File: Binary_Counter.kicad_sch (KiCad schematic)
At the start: 12 parts, among them SW1 SW_Push, U1 CH32V003FxUx

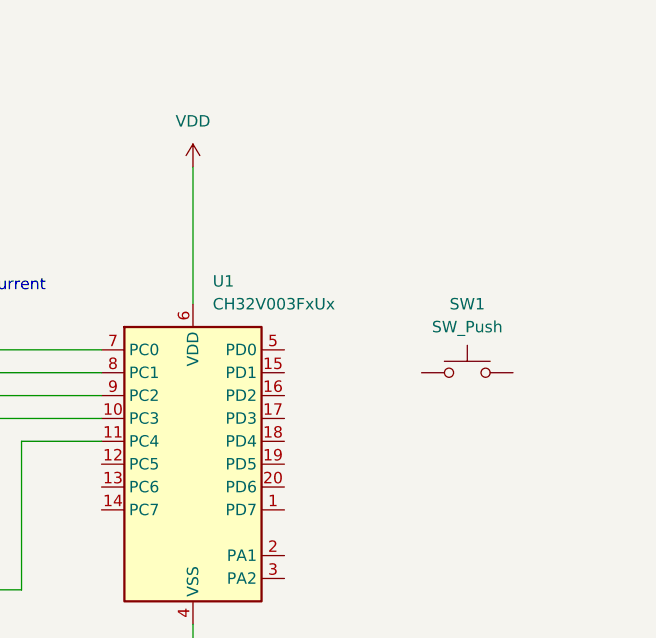
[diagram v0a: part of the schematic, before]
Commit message: move switch to PD2, add debouncing to switch
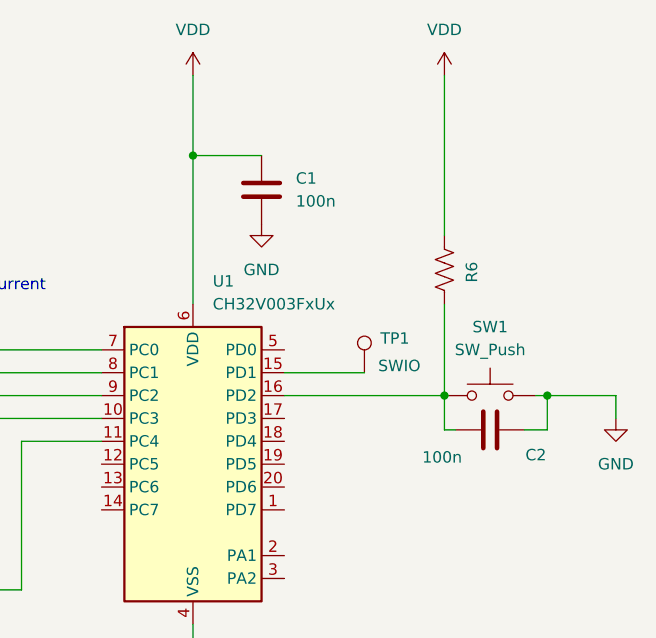
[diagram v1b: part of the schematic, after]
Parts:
- added C1, C2: 100n, symbol Device:C
- added R6: R_US, symbol Device:R_US
- added TP1: SWIO, symbol Connector:TestPoint
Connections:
- net GND: now also SW1.2, C1.2, C2.2
- net VDD: now also C1.1, R6.1
- net at SW1.1: now also U1.16 (PD2), C2.1, R6.2
- net at U1.15 (PD1): now also TP1.1

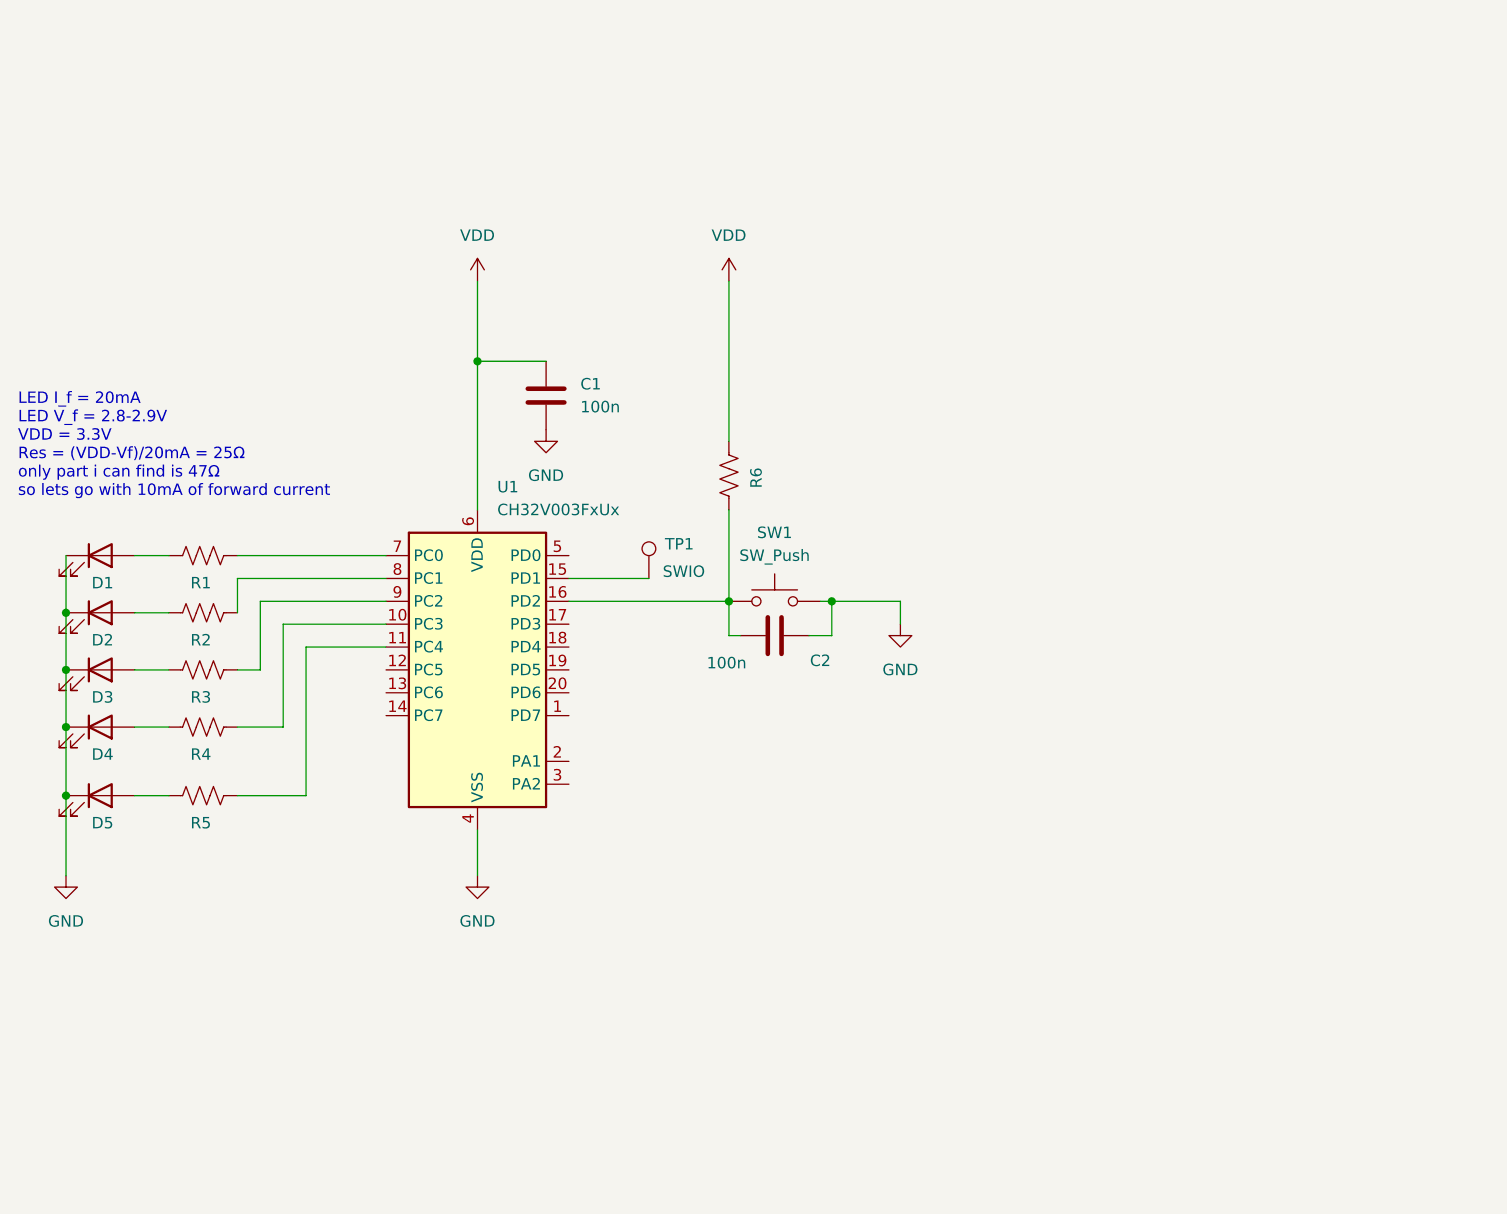
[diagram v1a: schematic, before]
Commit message: add 8 LEDs total and add a 3 pin connector for power and SWIO
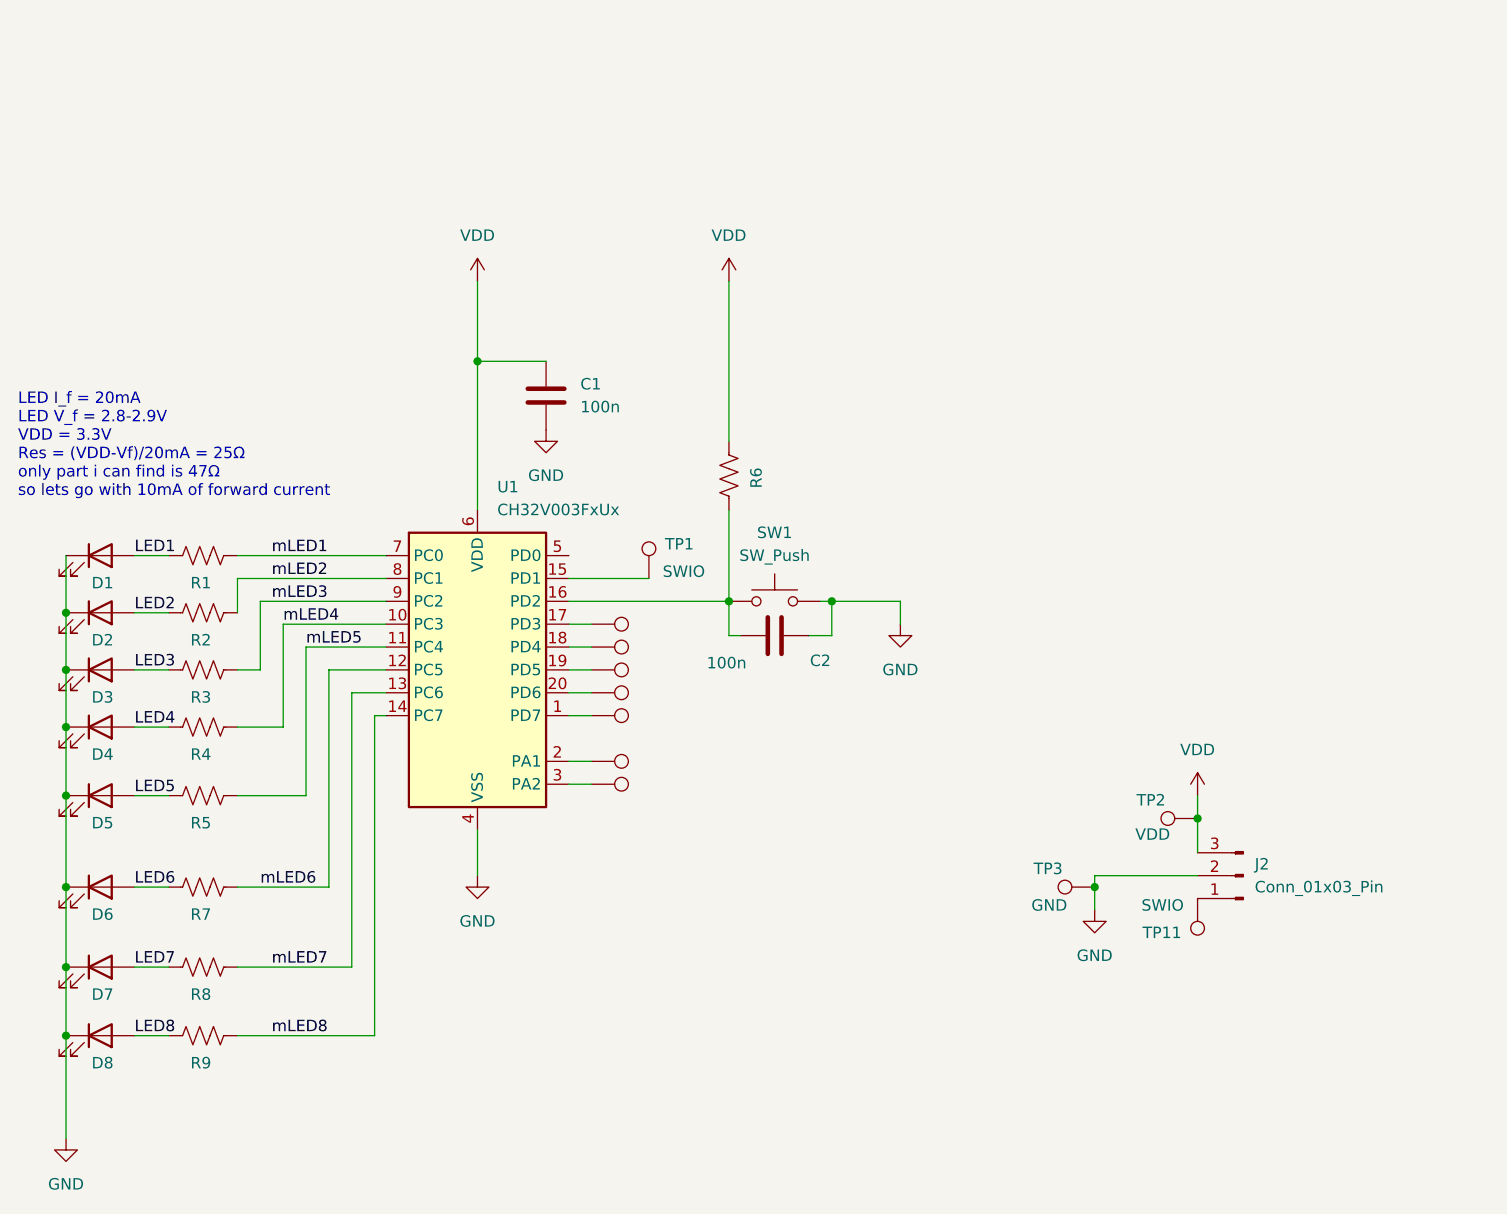
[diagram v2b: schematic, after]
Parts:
- added D6, D7, D8: LED, symbol Device:LED
- added J2: Conn_01x03_Pin, symbol Connector:Conn_01x03_Pin
- added R7, R8, R9: R_US, symbol Device:R_US
- added TP10, TP11, TP4, TP5, TP6, TP7, TP8, TP9: SWIO, symbol Connector:TestPoint
- added TP2: VDD, symbol Connector:TestPoint
- added TP3: GND, symbol Connector:TestPoint
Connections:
- net GND: now also D6.1 (K), D7.1 (K), D8.1 (K), J2.2 (Pin_2), TP3.1
- net VDD: now also J2.3 (Pin_3), TP2.1
- net LED4: now reaches D4.2 (A), R4.2
- net LED3: now reaches D3.2 (A), R3.2
- net mLED5: now reaches R5.1, U1.11 (PC4)
- net LED5: now reaches D5.2 (A), R5.2
- net mLED2: now reaches R2.1, U1.8 (PC1)
- net LED2: now reaches D2.2 (A), R2.2
- net LED1: now reaches D1.2 (A), R1.2
- net mLED4: now reaches R4.1, U1.10 (PC3)
- net mLED3: now reaches R3.1, U1.9 (PC2)
- net mLED1: now reaches R1.1, U1.7 (PC0)
- net at U1.1 (PD7): now also TP8.1
- net mLED6: now reaches U1.12 (PC5)
- net mLED6: now also R7.1
- net mLED7: now reaches U1.13 (PC6)
- net mLED7: now also R8.1
- net mLED8: now reaches U1.14 (PC7)
- net mLED8: now also R9.1
- net at U1.17 (PD3): now also TP4.1
- net at U1.18 (PD4): now also TP5.1
- net at U1.19 (PD5): now also TP6.1
- net at U1.2 (PA1): now also TP9.1
- net at U1.20 (PD6): now also TP7.1
- net at U1.3 (PA2): now also TP10.1
- new net: J2.1 (Pin_1), TP11.1
- new net LED6: D6.2 (A), R7.2
- new net LED7: D7.2 (A), R8.2
- new net LED8: D8.2 (A), R9.2

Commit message: initial placement of components on board
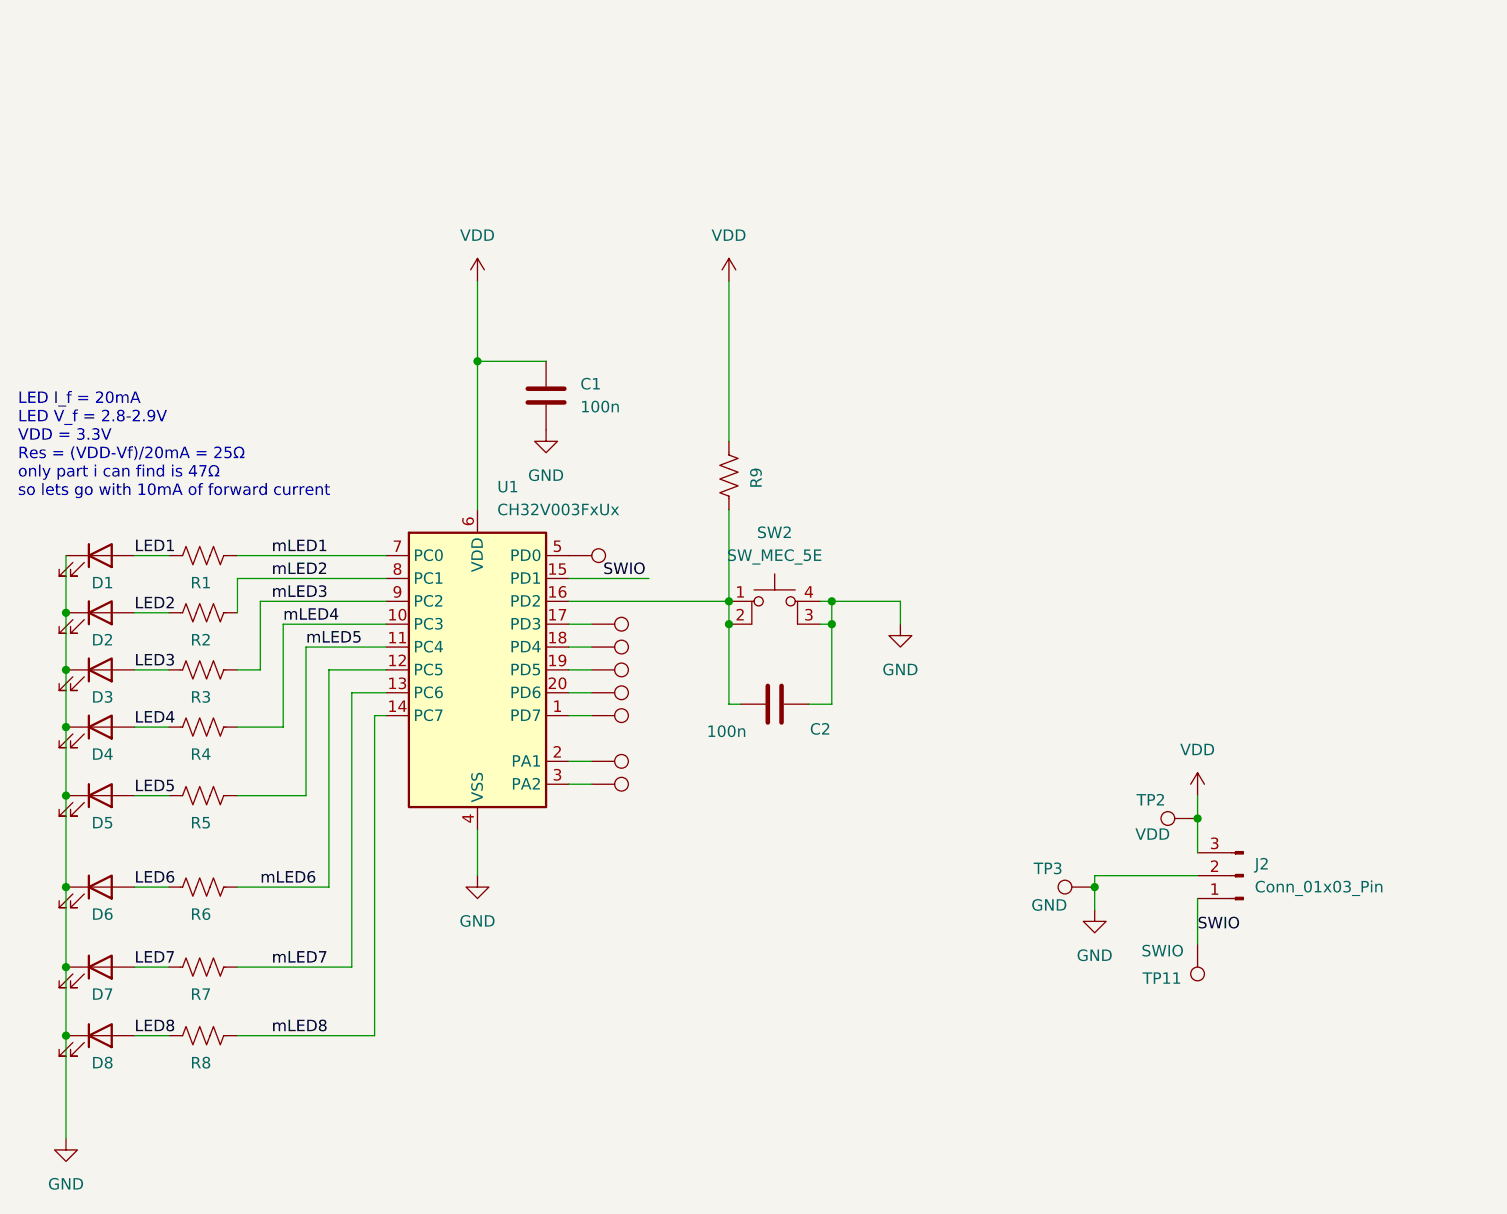
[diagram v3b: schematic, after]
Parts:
- removed SW1: SW_Push, symbol Switch:SW_Push
- removed TP1: SWIO, symbol Connector:TestPoint
- added SW2: SW_MEC_5E, TACT Switch:SW-SMD_4P-L5.1-W5.1-P3.70-LS6.5-TL-2, symbol Switch:SW_MEC_5E
- added TP12: PD0, TestPoint:TestPoint_Pad_D2.0mm, symbol Connector:TestPoint
- C1, C2: footprint (none) -> Capacitor_SMD:C_0805_2012Metric_Pad1.18x1.45mm_HandSolder
- D1, D2, D3, D4, D5, D6, D7, D8: footprint (none) -> LED:LED0805-R-RD
- J2: footprint (none) -> Connector:FanPinHeader_1x03_P2.54mm_Vertical
- R1, R2, R3, R4, R5: footprint (none) -> Resistor_SMD:R_0805_2012Metric_Pad1.20x1.40mm_HandSolder
- R6: renamed from R7; footprint (none) -> Resistor_SMD:R_0805_2012Metric_Pad1.20x1.40mm_HandSolder
- R7: renamed from R8; footprint (none) -> Resistor_SMD:R_0805_2012Metric_Pad1.20x1.40mm_HandSolder
- R8: renamed from R9; footprint (none) -> Resistor_SMD:R_0805_2012Metric_Pad1.20x1.40mm_HandSolder
- R9: renamed from R6; footprint (none) -> Resistor_SMD:R_0805_2012Metric_Pad1.20x1.40mm_HandSolder
- TP10: value SWIO -> PA2; footprint (none) -> TestPoint:TestPoint_Pad_D2.0mm
- TP11: footprint (none) -> TestPoint:TestPoint_Pad_D2.0mm
- TP2, TP3: footprint (none) -> TestPoint:TestPoint_Pad_D4.0mm
- TP4: value SWIO -> PD3; footprint (none) -> TestPoint:TestPoint_Pad_D2.0mm
- TP5: value SWIO -> OPO; footprint (none) -> TestPoint:TestPoint_Pad_D2.0mm
- TP6: value SWIO -> PD5; footprint (none) -> TestPoint:TestPoint_Pad_D2.0mm
- TP7: value SWIO -> PD6; footprint (none) -> TestPoint:TestPoint_Pad_D2.0mm
- TP8: value SWIO -> PD7; footprint (none) -> TestPoint:TestPoint_Pad_D2.0mm
- TP9: value SWIO -> PA1; footprint (none) -> TestPoint:TestPoint_Pad_D2.0mm
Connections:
- net GND: now also SW2.3 (K), SW2.4 (A)
- net at C2.1, R9.2, U1.16 (PD2): now also SW2.1, SW2.2
- net SWIO: now reaches J2.1 (Pin_1), TP11.1
- net SWIO: now also U1.15 (PD1)
- net at U1.5 (PD0): now also TP12.1
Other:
- moved on the sheet: C2, TP11

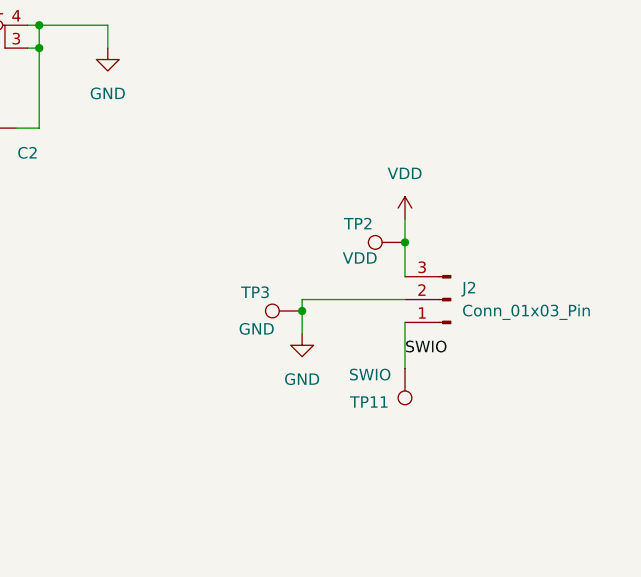
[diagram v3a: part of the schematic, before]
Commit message: complete routing
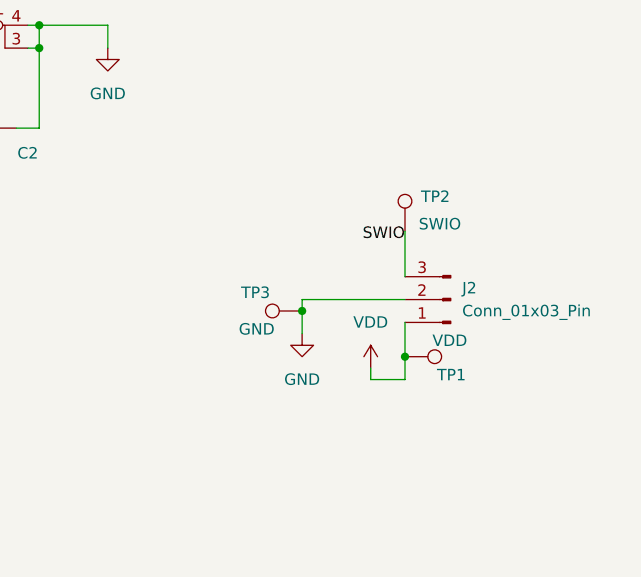
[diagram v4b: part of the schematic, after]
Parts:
- removed TP11: SWIO, TestPoint:TestPoint_Pad_D2.0mm, symbol Connector:TestPoint
- added TP1: VDD, TestPoint:TestPoint_Pad_D2.0mm, symbol Connector:TestPoint
- TP2: value VDD -> SWIO; footprint TestPoint:TestPoint_Pad_D4.0mm -> TestPoint:TestPoint_Pad_D2.0mm
- TP3: footprint TestPoint:TestPoint_Pad_D4.0mm -> TestPoint:TestPoint_Pad_2.0x2.0mm
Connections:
- net SWIO: now also J2.3 (Pin_3), TP2.1; no longer J2.1 (Pin_1)
- net VDD: now also J2.1 (Pin_1), TP1.1; no longer J2.3 (Pin_3), TP2.1

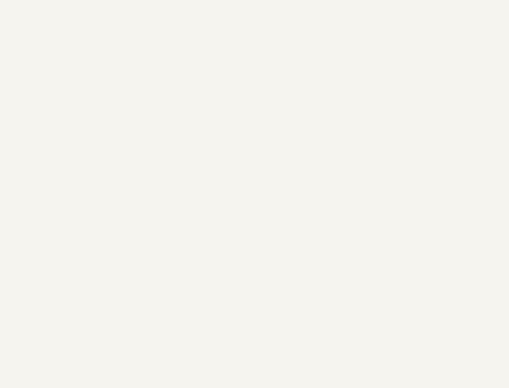
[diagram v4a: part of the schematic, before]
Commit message: add M2 mounting holes
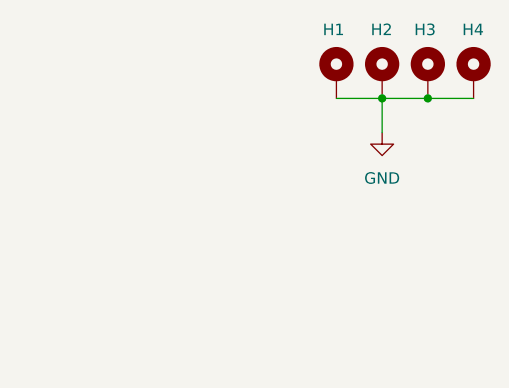
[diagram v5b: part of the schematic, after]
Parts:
- added H1, H2, H3, H4: MountingHole_Pad, MountingHole:MountingHole_4mm_Pad, symbol Mechanical:MountingHole_Pad
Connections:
- net GND: now also H1.1, H2.1, H3.1, H4.1
